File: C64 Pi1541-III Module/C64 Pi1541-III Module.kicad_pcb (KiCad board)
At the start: 2 copper layers, 100 x 100 mm, 25 parts, among them J1 DC IN, J2 C64_IEC, J3 C64_IEC, J8 Module_Panel, M1 Mounting, M2 Mounting, M3 Mounting, M4 Mounting, U1 7406

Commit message: ...
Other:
- net class Default removed
- net class Power removed

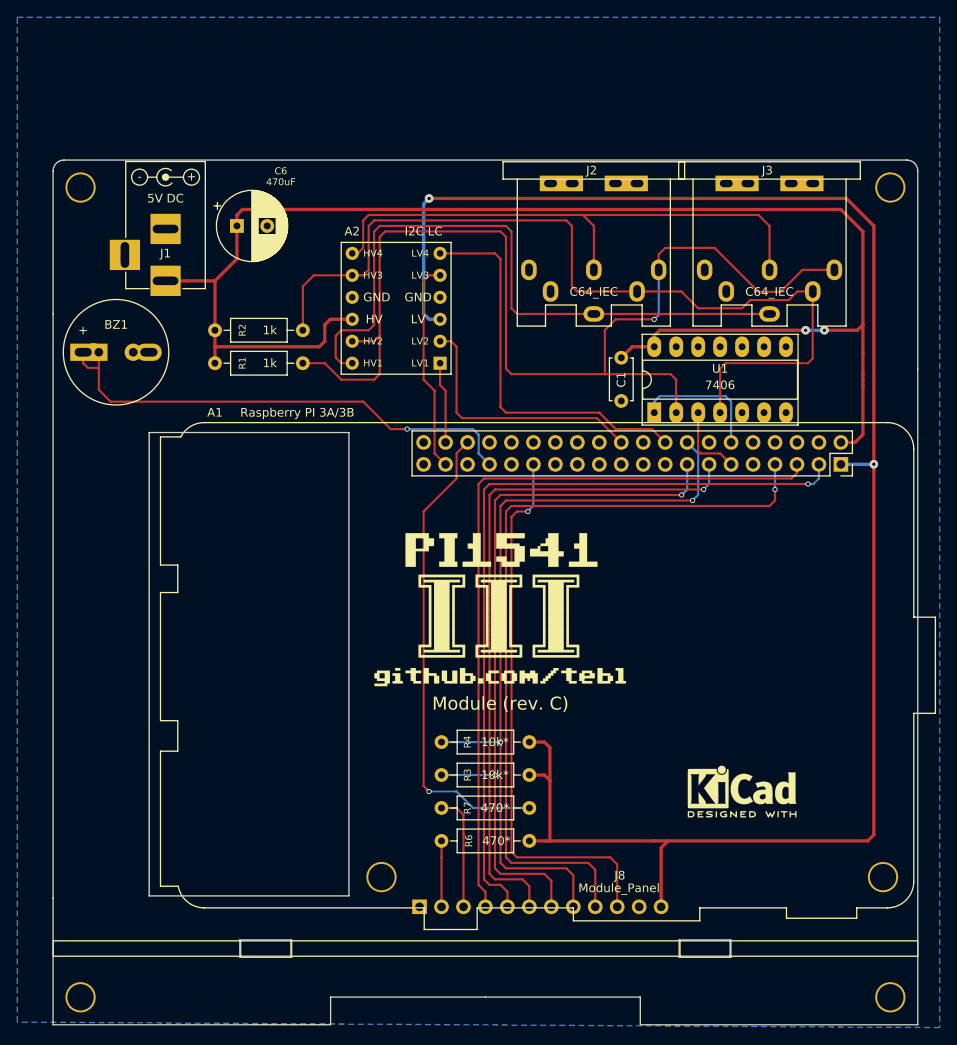
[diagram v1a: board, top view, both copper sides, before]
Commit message: SMD option for Pi1541-III
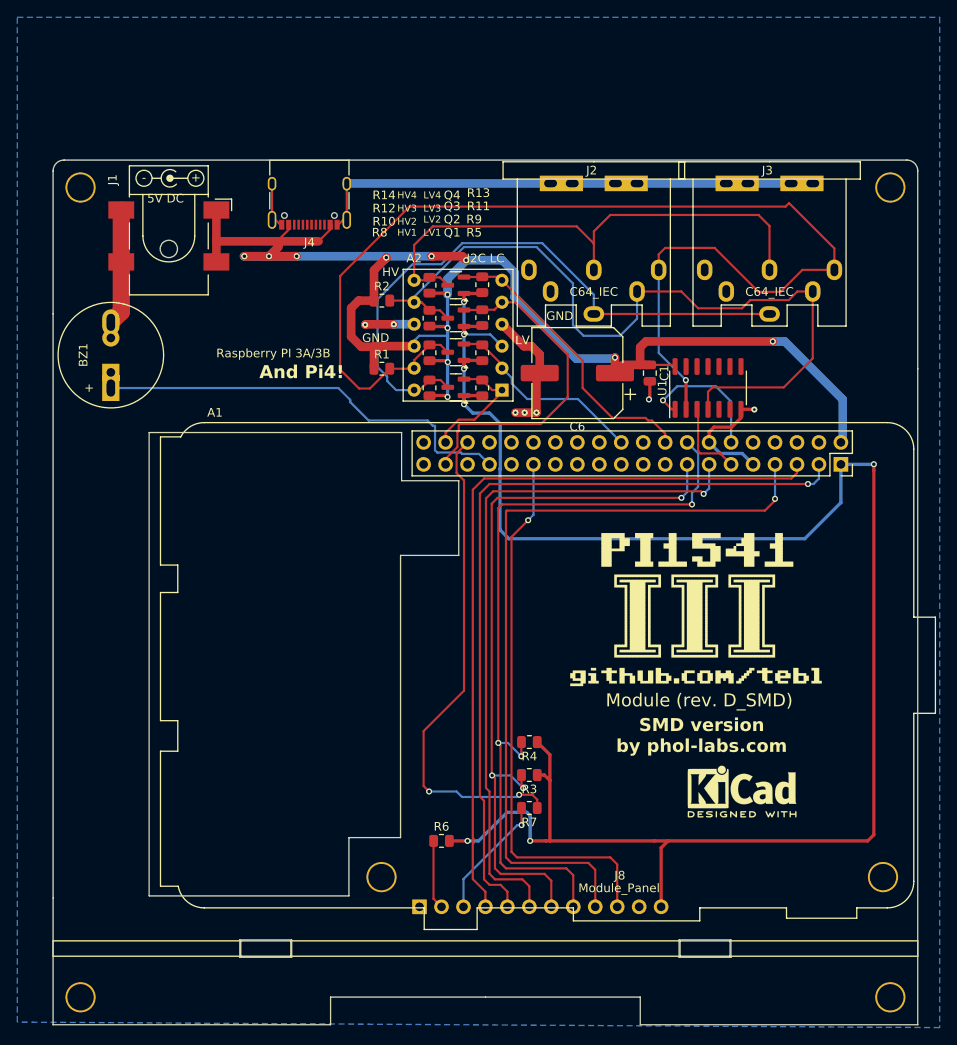
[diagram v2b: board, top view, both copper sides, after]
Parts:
- added J4: USB_C_Receptacle_USB2.0, Connector_USB:USB_C_Receptacle_XKB_U262-16XN-4BVC11, F.Cu at (99.8, 58.4)
- added Q1: DMG2302U, Package_TO_SOT_SMD:SOT-23, F.Cu at (116.8, 80.9)
- added Q2: DMG2302U, Package_TO_SOT_SMD:SOT-23, F.Cu at (116.8, 76.8)
- added Q3: DMG2302U, Package_TO_SOT_SMD:SOT-23, F.Cu at (116.8, 72.9)
- added Q4: DMG2302U, Package_TO_SOT_SMD:SOT-23, F.Cu at (116.8, 69.1)
- added R10: 10k*, Resistor_SMD:R_0805_2012Metric, F.Cu at (113.7, 76.9)
- added R11: 10k*, Resistor_SMD:R_0805_2012Metric, F.Cu at (119.8, 72.8)
- added R12: 10k*, Resistor_SMD:R_0805_2012Metric, F.Cu at (113.7, 72.9)
- added R13: 10k*, Resistor_SMD:R_0805_2012Metric, F.Cu at (119.8, 69.0)
- added R14: 10k*, Resistor_SMD:R_0805_2012Metric, F.Cu at (113.7, 69.1)
- added R5: 10k*, Resistor_SMD:R_0805_2012Metric, F.Cu at (119.8, 81.0)
- added R8: 10k*, Resistor_SMD:R_0805_2012Metric, F.Cu at (113.7, 81.0)
- added R9: 10k*, Resistor_SMD:R_0805_2012Metric, F.Cu at (119.8, 76.9)
- C1: footprint Capacitor_THT:C_Disc_D4.7mm_W2.5mm_P5.00mm -> Capacitor_SMD:C_0805_2012Metric
- C6: footprint Capacitor_THT:CP_Radial_D8.0mm_P3.50mm -> Capacitor_SMD:CP_Elec_10x7.7
- J1: footprint pi1541:BARREL_JACK -> Connector_BarrelJack:BarrelJack_CLIFF_FC681465S_SMT_Horizontal
- R1, R2, R3, R4, R6, R7: footprint resistor:R_Axial_DIN0207_L6.3mm_D2.5mm_P10.16mm_Horizontal -> Resistor_SMD:R_0805_2012Metric
- U1: footprint Package_DIP:DIP-14_W7.62mm_Socket_LongPads -> Package_SO:SO-14_3.9x8.65mm_P1.27mm
- moved C6 42.9 mm to (130.8, 79.2), turned to 180 degrees
- moved G*** 22.6 mm to (124.9, 97.1)
- moved R2 19.6 mm to (108.2, 70.9)
- moved R1 19.3 mm to (108.2, 78.7)
- moved A2 7.81 mm to (117.0, 76.1)
- moved U1 6.85 mm to (145.9, 81.0)
- moved BZ1 5.23 mm to (76.9, 81.0), turned to 90 degrees
- moved J1 5.21 mm to (83.6, 63.4)
- moved C1 3.75 mm to (139.2, 79.2)
- moved SYM1 0.52 mm to (83.7, 56.6)
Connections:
- A1 pad 10: (no net) -> unconnected-(A1-GPIO15/RXD-Pad10)
- A1 pad 17: (no net) -> unconnected-(A1-3V3-Pad17)
- A1 pad 19: (no net) -> unconnected-(A1-MOSI0/GPIO10-Pad19)
- A1 pad 21: (no net) -> unconnected-(A1-MISO0/GPIO9-Pad21)
- A1 pad 23: (no net) -> unconnected-(A1-SCLK0/GPIO11-Pad23)
- A1 pad 24: (no net) -> unconnected-(A1-~{CE0}/GPIO8-Pad24)
- A1 pad 26: (no net) -> unconnected-(A1-~{CE1}/GPIO7-Pad26)
- A1 pad 27: (no net) -> unconnected-(A1-ID_SD/GPIO0-Pad27)
- A1 pad 28: (no net) -> unconnected-(A1-ID_SC/GPIO1-Pad28)
- A1 pad 31: (no net) -> unconnected-(A1-GCLK2/GPIO6-Pad31)
- A1 pad 32: (no net) -> unconnected-(A1-PWM0/GPIO12-Pad32)
- A1 pad 35: (no net) -> unconnected-(A1-GPIO19/MISO1-Pad35)
- A1 pad 4: (no net) -> unconnected-(A1-5V-Pad4)
- A1 pad 40: (no net) -> unconnected-(A1-GPIO21/SCLK1-Pad40)
- A1 pad 8: (no net) -> unconnected-(A1-GPIO14/TXD-Pad8)
- J2 pad 1: (no net) -> unconnected-(J2-Pad1)
- J3 pad 1: (no net) -> unconnected-(J3-Pad1)
- U1 pad 10: (no net) -> unconnected-(U1-5Y-Pad10)
- U1 pad 11: (no net) -> unconnected-(U1-5A-Pad11)
- U1 pad 12: (no net) -> unconnected-(U1-6Y-Pad12)
- U1 pad 13: (no net) -> unconnected-(U1-6A-Pad13)
- U1 pad 5: (no net) -> unconnected-(U1-3A-Pad5)
- U1 pad 6: (no net) -> unconnected-(U1-3Y-Pad6)
- U1 pad 8: (no net) -> unconnected-(U1-4Y-Pad8)
- U1 pad 9: (no net) -> unconnected-(U1-4A-Pad9)
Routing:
- net GND: track 1.81 -> 115.4 mm, vias 0 -> 7
- net RPI_CLK_IN: track 24.4 -> 38.9 mm
- net RPI_ATN: track 45.1 -> 33.6 mm
- net C64_CLK: track 103.3 -> 92.8 mm
- net C64_DATA: track 126.5 -> 135.5 mm
- net Net-(A1-PWM1/GPIO13): track 57.7 -> 49.3 mm, vias 1 -> 0
- net +3V3: track 206.9 -> 214.7 mm, vias 2 -> 7
- net RPI_DATA_IN: track 30.3 -> 23.5 mm
- net RPI_RST: track 9.42 -> 14.7 mm
- net C64_RST: track 75.9 -> 70.9 mm
- net +5V: track 172.6 -> 177.4 mm, vias 2 -> 12
- net RPI_LED: track 55.1 -> 57.5 mm, vias 1 -> 2
- net C64_ATN: track 64.4 -> 62.1 mm
- net SW3_DOWN: track 90.7 -> 89.3 mm, vias 2 -> 3
- net LED_ACT: track 13.5 -> 14.5 mm, vias 0 -> 1
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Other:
- outline, holes or cut-outs redrawn
- board text added: "And Pi4!"
- board text added: "Module (rev. D_SMD)"
- board text added: "SMD version by phol-labs.com"
- board text removed: "Module (rev. C)"
